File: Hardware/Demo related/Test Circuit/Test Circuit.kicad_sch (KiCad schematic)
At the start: 60 parts, among them U1 MCP2518FD-xQBB, U2 MCP2518FD-xQBB, U3 TCAN337, U4 TCAN337, U5 MCP2518FD-xQBB, U6 TCAN337, Y1 40MHz Crystal, Y2 40MHz Crystal, Y3 40MHz Crystal

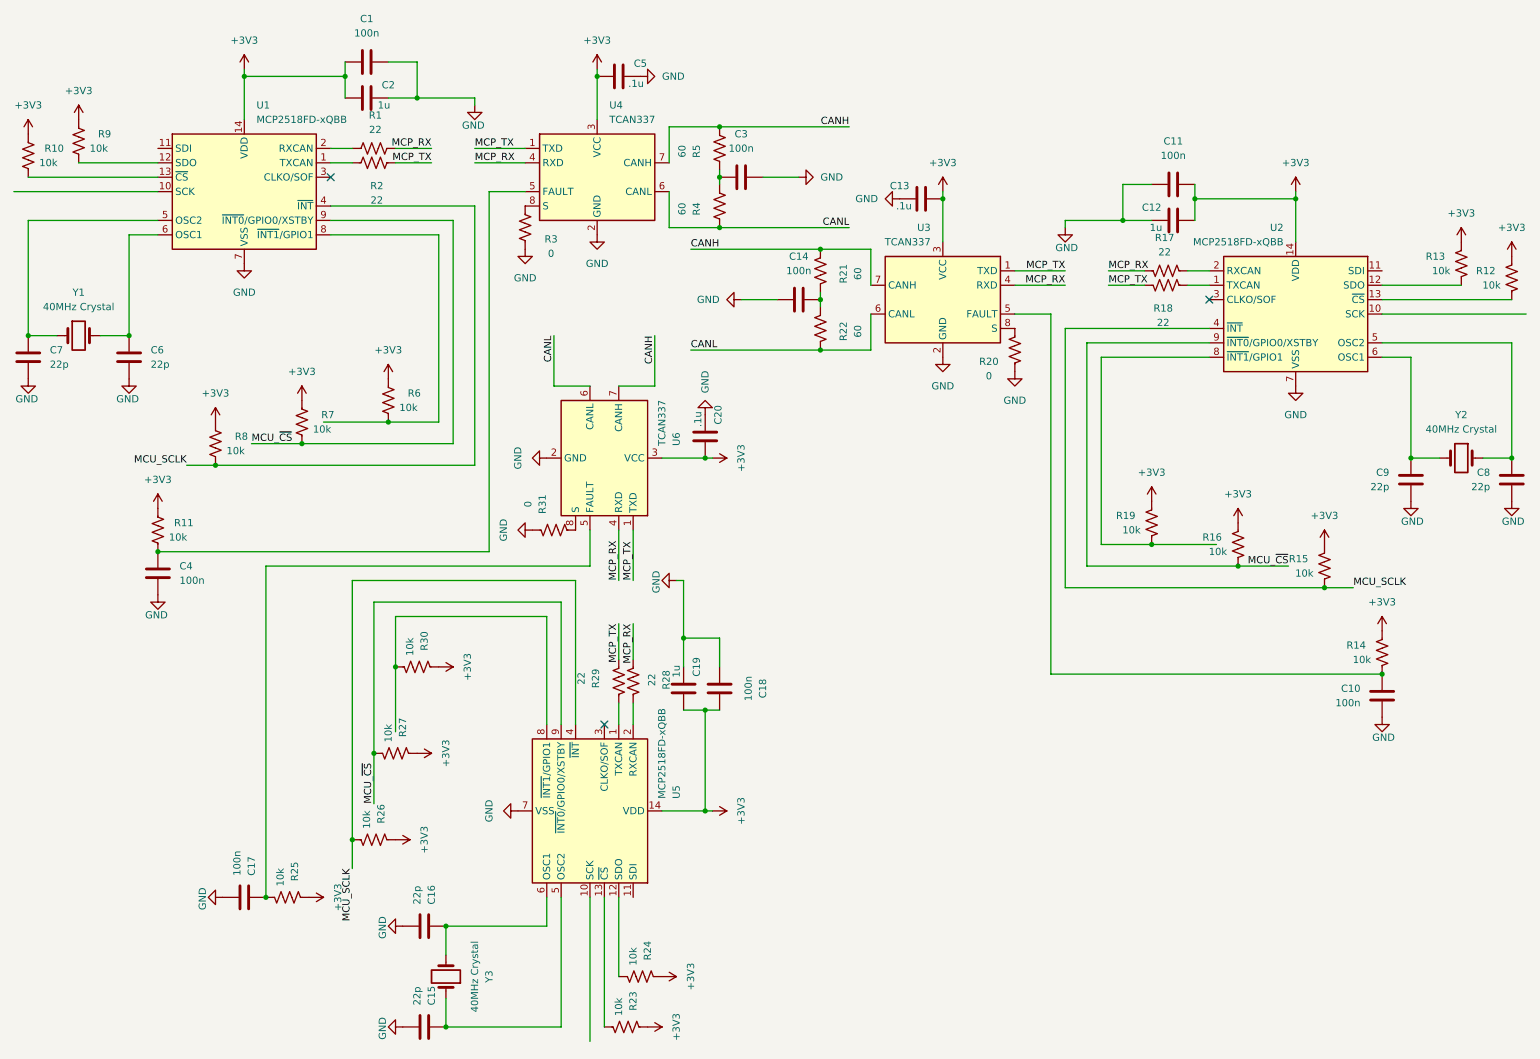
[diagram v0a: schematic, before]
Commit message: Rev2 PCB finished, need to document and catalog for Iowa Innovation challenge this thursday
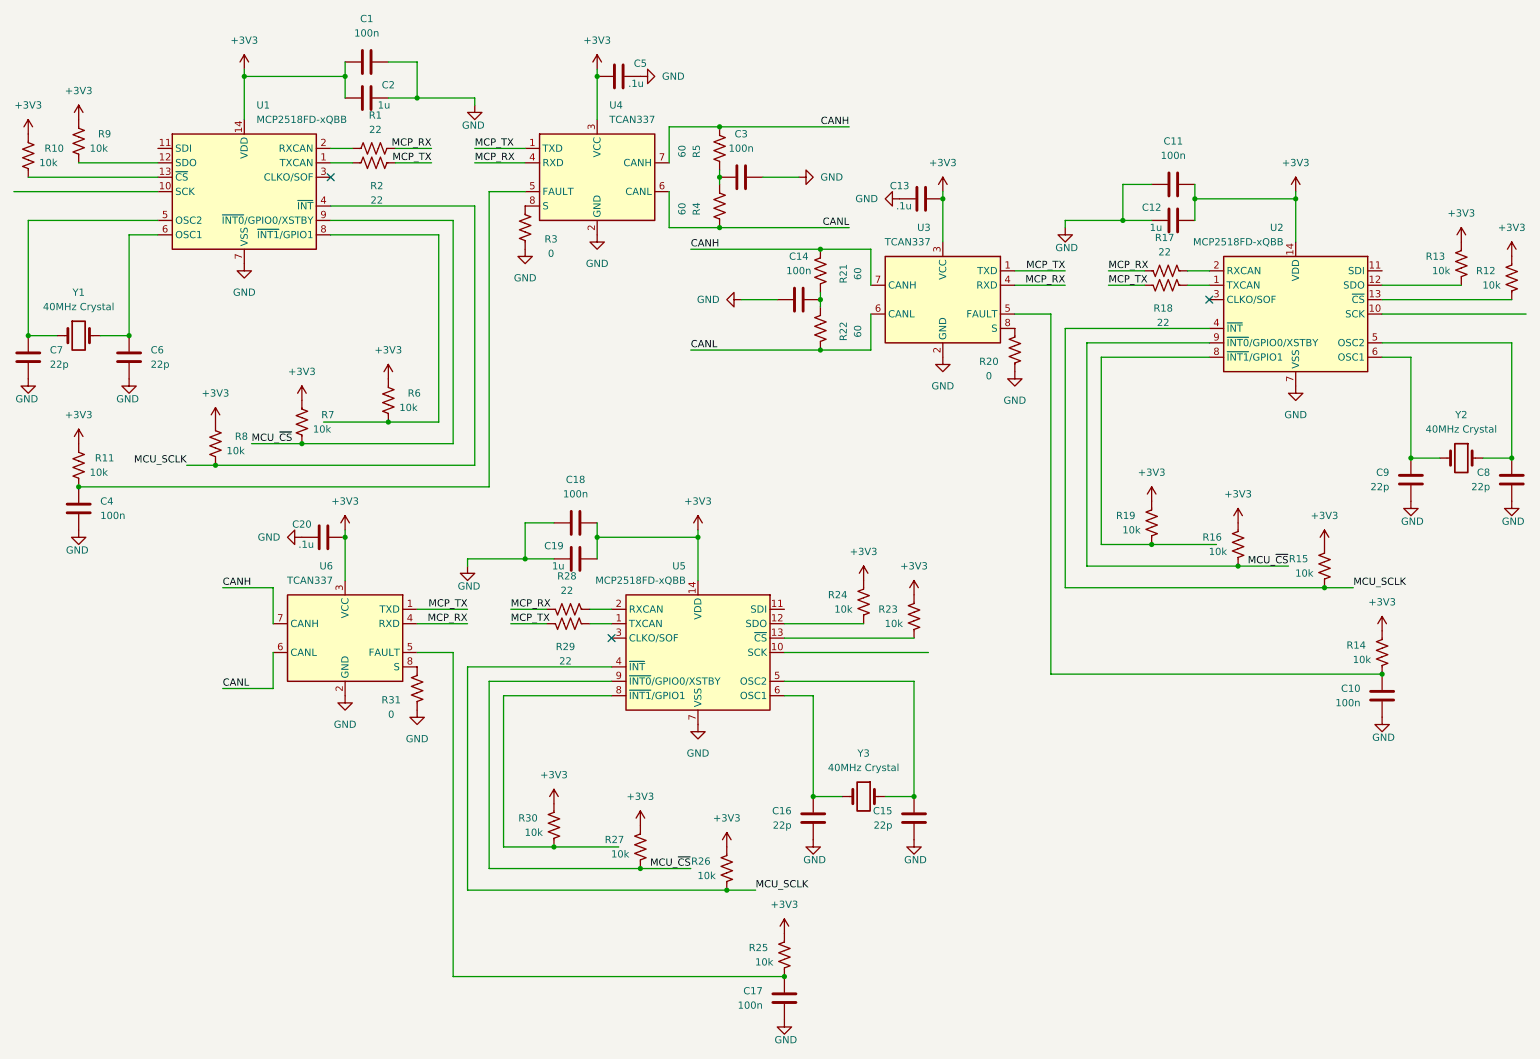
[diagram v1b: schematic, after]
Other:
- moved on the sheet: C15, C16, C17, C18, C19, C20, C4, R11, R23, R24, R25, R26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
